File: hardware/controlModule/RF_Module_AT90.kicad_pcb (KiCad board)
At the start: 2 copper layers, 44 x 44 mm, 24 parts, among them IC1 ATMEGA8535-A, P1 CONN_02X10, P2 CONN_02X10, P3 CONN_02X03, SW1 SW_PUSH, U1 LM317AEMP, X1 CRYSTAL, X1 P***, X2 P***

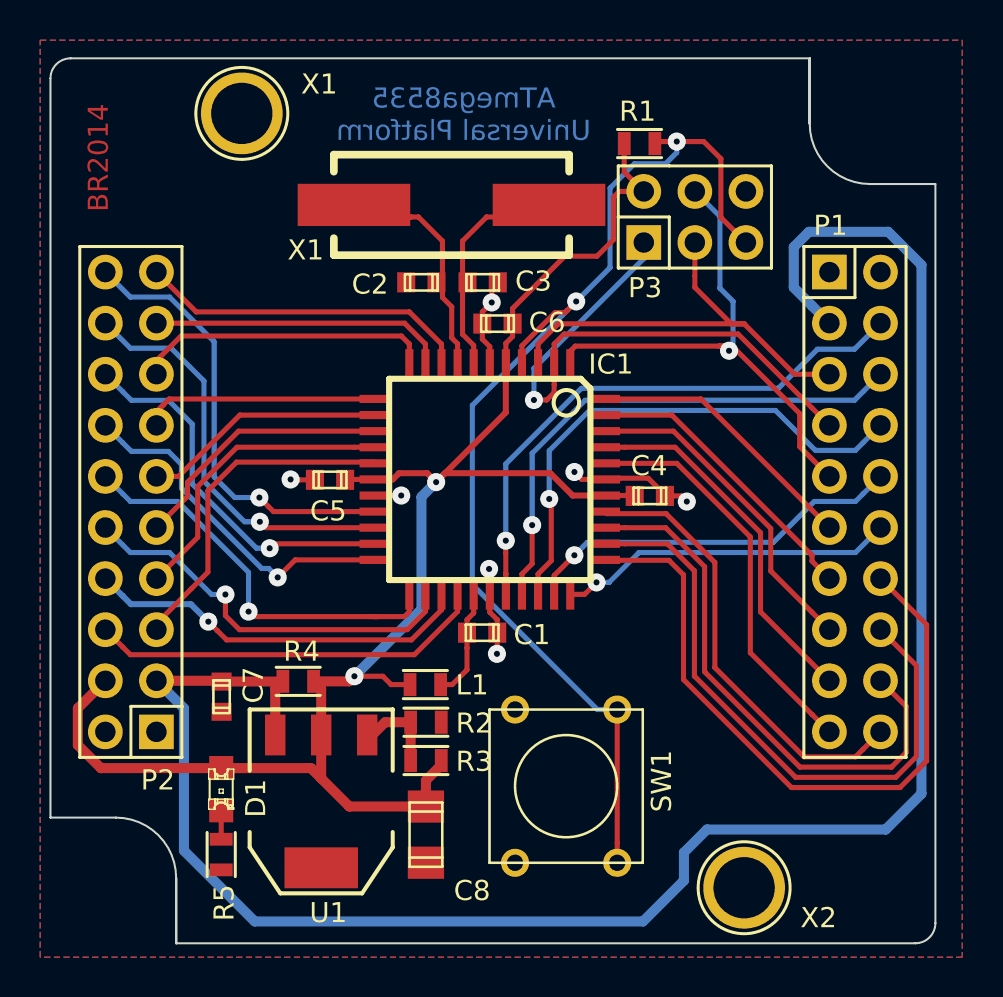
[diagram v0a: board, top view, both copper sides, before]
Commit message: modification on main control pcb
moved main connectors to fit into an imperial grid
modified routings to main connector p1
decreased width of vdd route to connector p2
added revision to copper text field
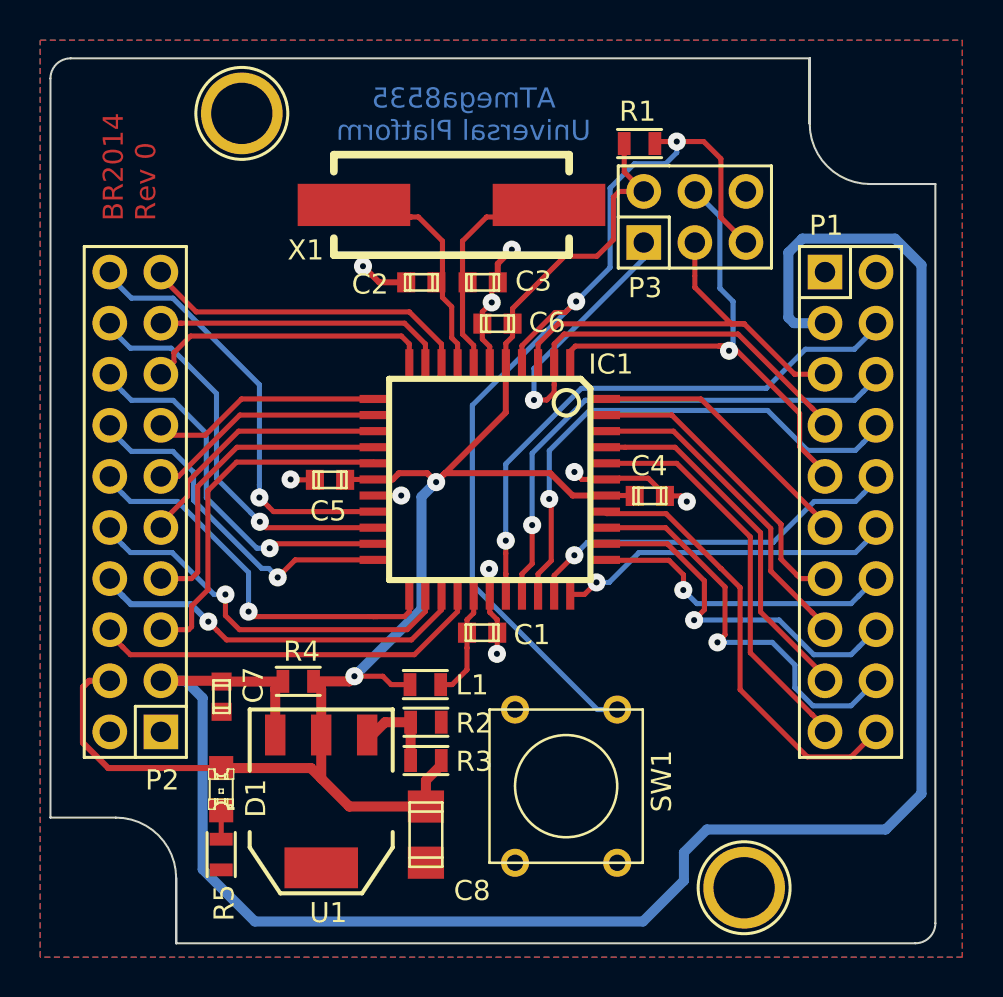
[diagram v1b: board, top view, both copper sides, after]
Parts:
- moved P1 0.22 mm to (157.9, 93.6)
- moved P2 0.22 mm to (122.3, 93.6)
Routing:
- net /PA3: track 34.3 -> 15.4 mm, vias 0 -> 1
- net /PA2: track 30.8 -> 18.2 mm, vias 0 -> 1
- net /RESET_N: track 57.4 -> 49.8 mm
- net /PA1: track 27.4 -> 20.5 mm, vias 0 -> 1
- net GND: track 17.9 -> 22.3 mm, vias 7 -> 9
- net /V_EXT: track 97.9 -> 99.3 mm
- net /PD7: track 17.6 -> 18.6 mm
- net /PD6: track 15.7 -> 16.5 mm
- net /PC0: track 22.3 -> 21.6 mm
- net /PB3: track 14.7 -> 15.3 mm
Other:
- board text added: "0"
- board text added: "16.12.2014"
- board text added: "AT90S8535 Control Board"
- board text added: "BR2014 Rev 0"
- board text removed: "BR2014"
